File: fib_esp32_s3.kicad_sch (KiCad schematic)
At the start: 1 part, among them U4 ESP32-S3-WROOM-1U

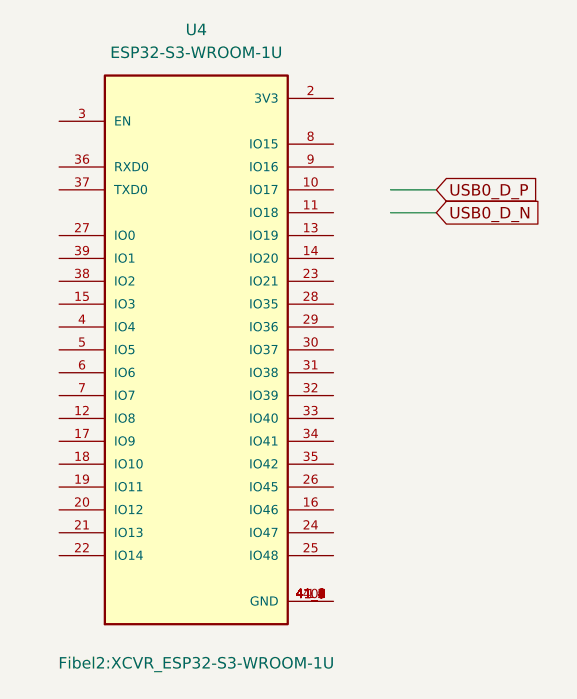
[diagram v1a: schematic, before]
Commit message: partially implemented E-INK PMIC
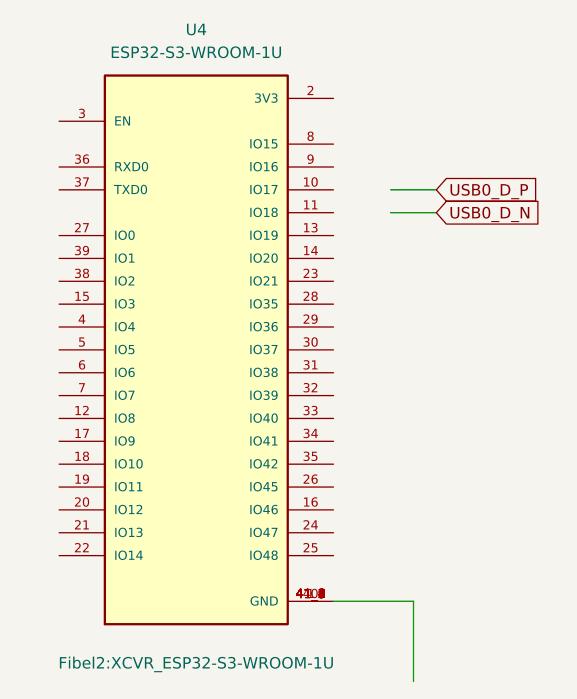
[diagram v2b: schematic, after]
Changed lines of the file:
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@@
+	(wire
+		(pts
+			(xy 127 130.81) (xy 127 139.7)
+		)
+		(stroke
+			(width 0)
+			(type default)
+		)
+	)
 	(wire
 		(pts
@@
 		)
 		(stroke
+			(width 0)
+			(type default)
+		)
+	)
+	(wire
+		(pts
+			(xy 118.11 130.81) (xy 127 130.81)
+		)
+		(stroke
